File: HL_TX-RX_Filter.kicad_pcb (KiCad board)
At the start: 2 copper layers, 100 x 100 mm, 200 parts, among them J1 CNR1, J10 To Rx in, J11 CONN_01X03, J2 CNR3, J3 Antenna, J4 CNR2, J5 CNR4, J6 From Tx, J7 ICSP, J8 CONN_01X05, J9 SCL SDA, Q1 2N7002, Q2 2N7002, Q3 2N7002, Q4 2N7002, Q5 2N7002, Q6 2N7002, Q7 2N7002, Q8 2N7002, U1 ATMEGA328-AU, U10 PE4259, U11 PE4259, U12 PE4259, U2 PE4259, U3 PE4259, U4 PE4259, U5 PE4259, U6 PE4259, U7 PE4259, U8 PE4259, U9 PE4259

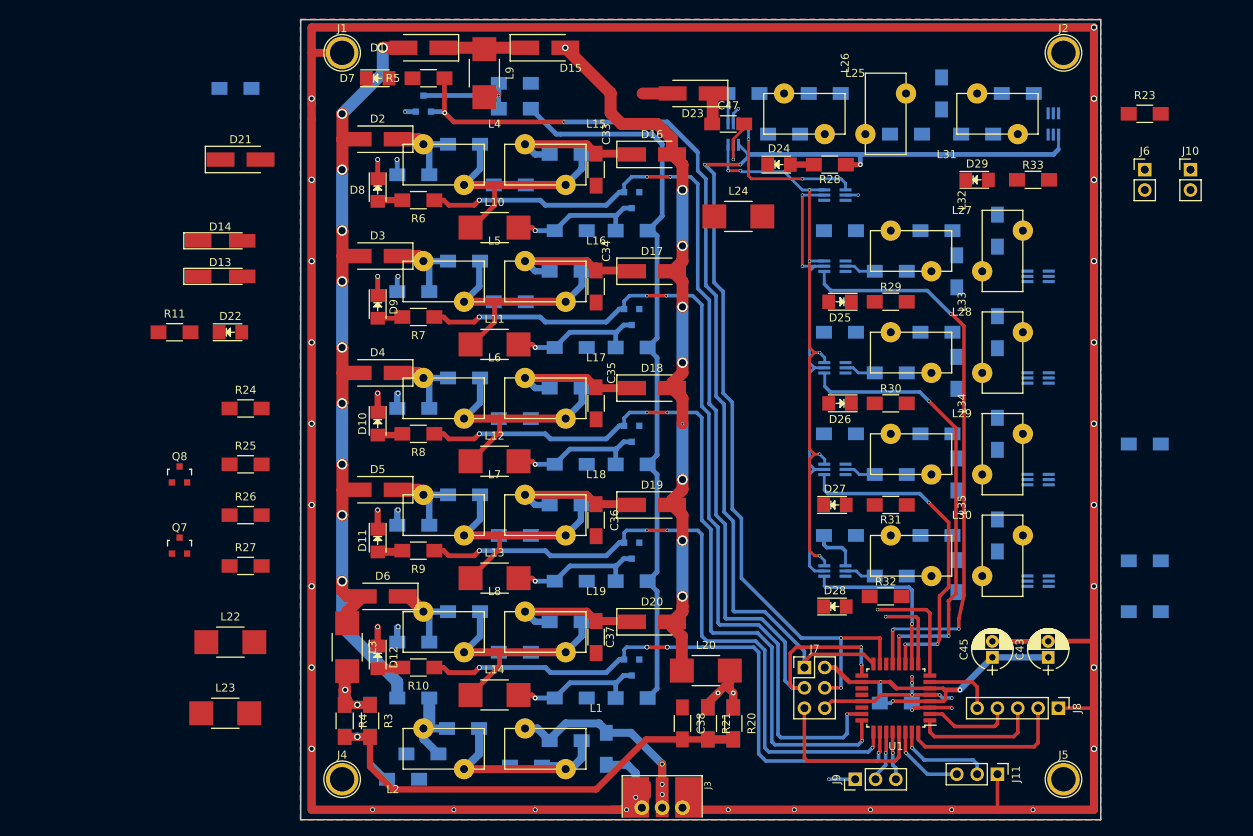
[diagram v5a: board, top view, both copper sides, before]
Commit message: Add Tx/Rx changeover components
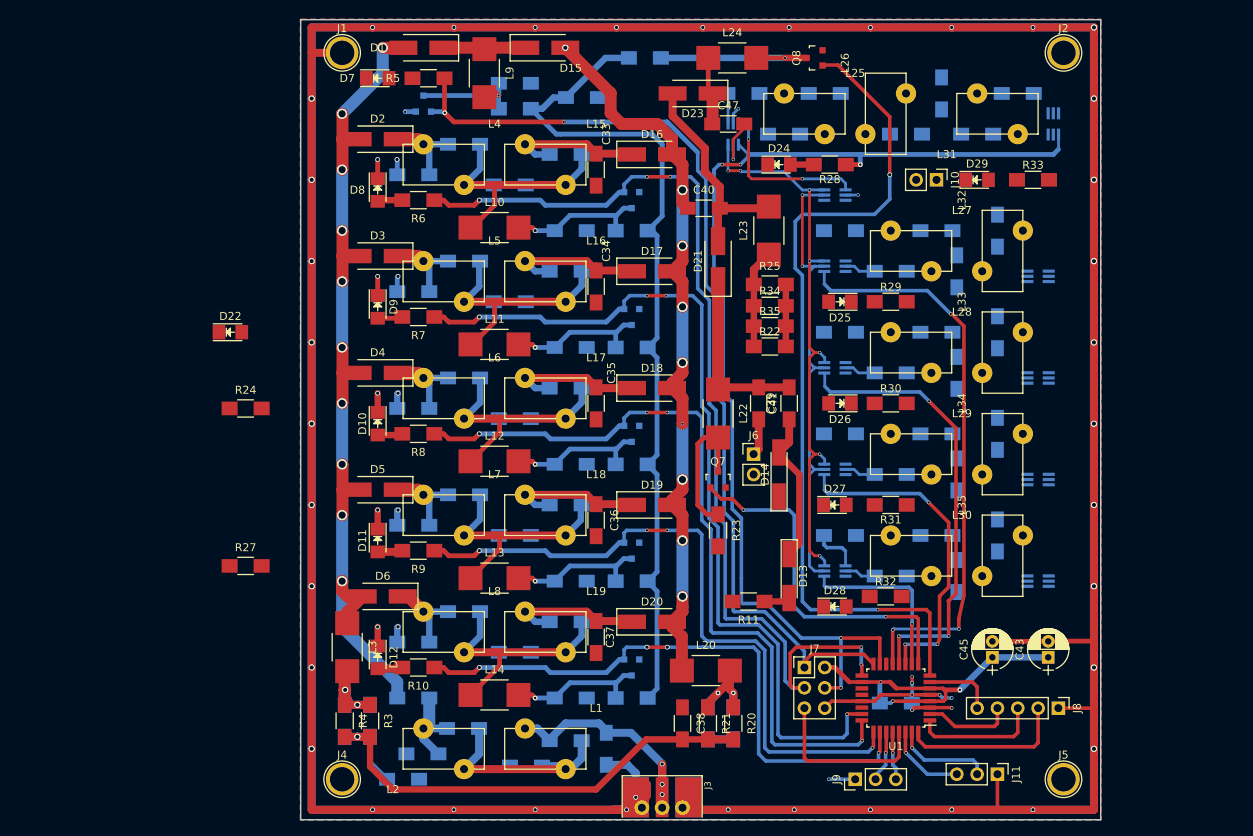
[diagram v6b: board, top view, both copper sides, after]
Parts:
- added R22: 680, Resistors_SMD:R_1206_HandSoldering, F.Cu at (183.6, 100.8)
- added R34: 680, Resistors_SMD:R_1206_HandSoldering, F.Cu at (183.6, 95.8)
- added R35: 680, Resistors_SMD:R_1206_HandSoldering, F.Cu at (183.6, 98.3)
- C39, C40, C41: moved to F.Cu
- R1, R18, R19, R2, R20, R21, R25, R3, R4: value R -> 680
- R26: moved to B.Cu
- moved Q8 94.9 mm to (189.2, 64.8), turned to 90 degrees
- moved C46 91.1 mm to (160.1, 69.7)
- moved L23 90.9 mm to (183.5, 86.4), turned to 90 degrees
- moved D13 80.4 mm to (186.1, 129.5), turned to 270 degrees
- moved C39 79.6 mm to (186.1, 108.0), turned to 90 degrees
- moved R11 79.3 mm to (181.0, 132.7), turned to 180 degrees
- moved R26 75.9 mm to (168.0, 64.8), turned to 180 degrees
- moved D14 75.7 mm to (184.8, 116.8), turned to 90 degrees
- moved R23 74.5 mm to (177.2, 123.8), turned to 270 degrees
- moved R25 69.3 mm to (183.6, 93.1)
- moved Q7 67.8 mm to (177.2, 117.5)
- moved L22 67.3 mm to (177.2, 109.2), turned to 270 degrees
- moved C40 62.5 mm to (175.4, 83.6)
- moved D21 61.0 mm to (177.2, 90.2), turned to 90 degrees
- moved J6 60.5 mm to (181.6, 114.3)
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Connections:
- C38 pad 2: Net-(C38-Pad2) -> BiasV
- C6 pad 2: Net-(C38-Pad2) -> BiasV
- L23 pad 1: 3V3 -> Net-(L23-Pad1)
- L23 pad 2: Net-(L23-Pad2) -> Net-(C40-Pad2)
- R1 pad 2: Net-(C38-Pad2) -> BiasV
- R18 pad 2: Net-(C38-Pad2) -> BiasV
- R19 pad 2: Net-(C38-Pad2) -> BiasV
- R2 pad 2: Net-(C38-Pad2) -> BiasV
- R20 pad 2: Net-(C38-Pad2) -> BiasV
- R21 pad 2: Net-(C38-Pad2) -> BiasV
- R25 pad 1: Net-(L23-Pad2) -> Net-(L23-Pad1)
- R25 pad 2: Net-(C40-Pad2) -> BiasV
- R3 pad 2: Net-(C38-Pad2) -> BiasV
- R4 pad 2: Net-(C38-Pad2) -> BiasV
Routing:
- net /Rptt: track 14.5 -> 106.6 mm, vias 1 -> 2
- net BiasV: track 0.00 -> 76.4 mm, vias 0 -> 1
- net Net-(C38-Pad2): track 68.7 -> 0.00 mm, vias 1 -> 0
- net /Tptt: track 9.83 -> 45.2 mm, vias 1 -> 2
- net Net-(C40-Pad2): track 3.75 -> 27.2 mm
- net Net-(C39-Pad2): track 0.00 -> 22.9 mm
- net Net-(L24-Pad2): track 0.00 -> 21.8 mm, vias 0 -> 1
- net Net-(C39-Pad1): track 0.00 -> 18.9 mm
- net Net-(L22-Pad2): track 0.00 -> 17.8 mm
- net Net-(C46-Pad1): track 92.4 -> 107.3 mm
- net Net-(L23-Pad1): track 0.00 -> 12.3 mm
- net Net-(C47-Pad1): track 3.83 -> 8.50 mm
- net Net-(C41-Pad2): track 0.00 -> 4.61 mm
- net Net-(D13-Pad2): track 0.00 -> 3.26 mm
- net Net-(C40-Pad1): track 91.1 -> 93.6 mm
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
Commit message: More layout around bias voltage area
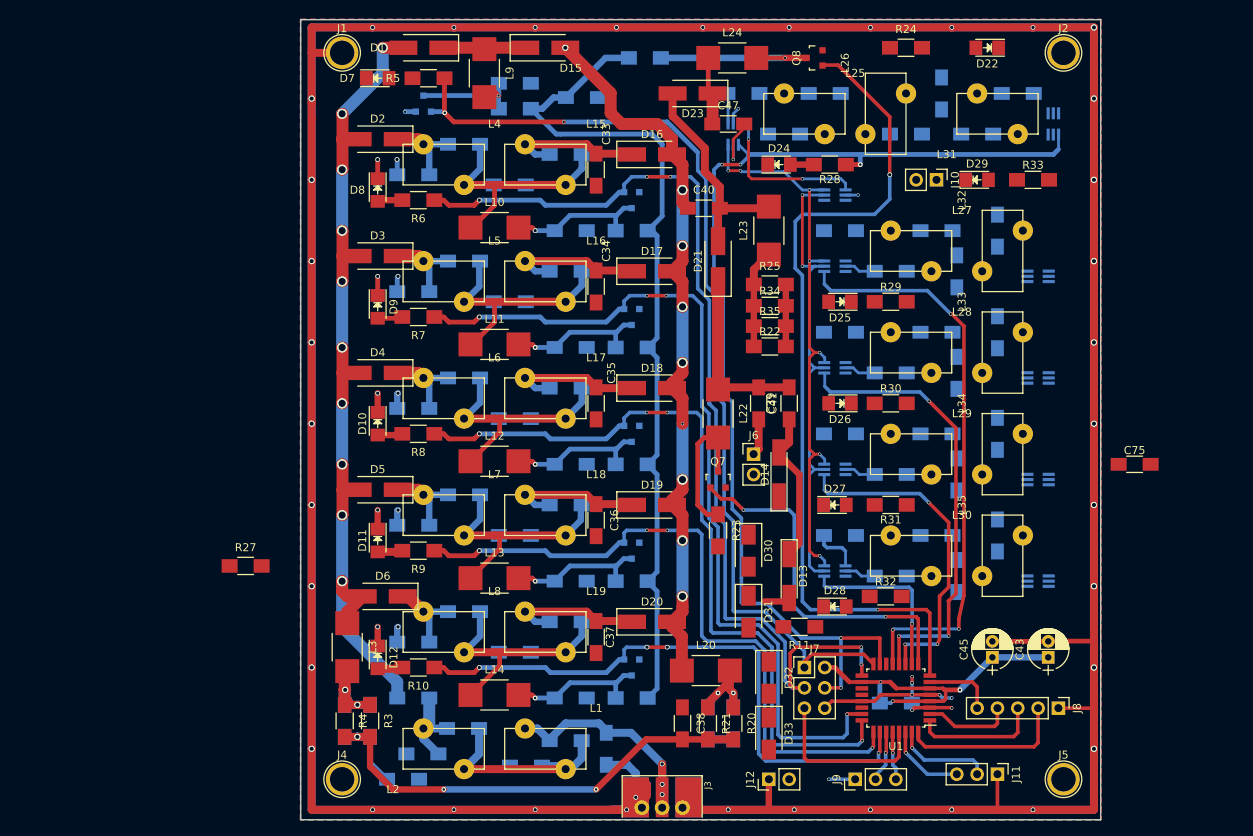
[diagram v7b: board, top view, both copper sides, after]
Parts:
- added C75: .1u, Capacitors_SMD:C_1206_HandSoldering, F.Cu at (229.2, 115.6)
- added D30: M7, Diodes_SMD:D_SMA, F.Cu at (181.0, 126.4)
- added D31: M7, Diodes_SMD:D_SMA, F.Cu at (181.0, 134.0)
- added D32: M7, Diodes_SMD:D_SMA, F.Cu at (183.5, 142.2)
- added D33: M7, Diodes_SMD:D_SMA, F.Cu at (183.5, 149.2)
- added J12: + - 12v, Pin_Headers:Pin_Header_Straight_1x02_Pitch2.54mm, F.Cu at (183.5, 154.9)
- moved D22 101.1 mm to (210.8, 63.5), turned to 180 degrees
- moved R24 94.1 mm to (200.7, 63.5)
- moved R11 7.10 mm to (187.3, 135.9)
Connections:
- R11 pad 2: +12V -> +12v
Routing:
- net GND: track 883.1 -> 886.9 mm
- net BiasV: vias 1 -> 3

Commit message: Got last of components placed on board
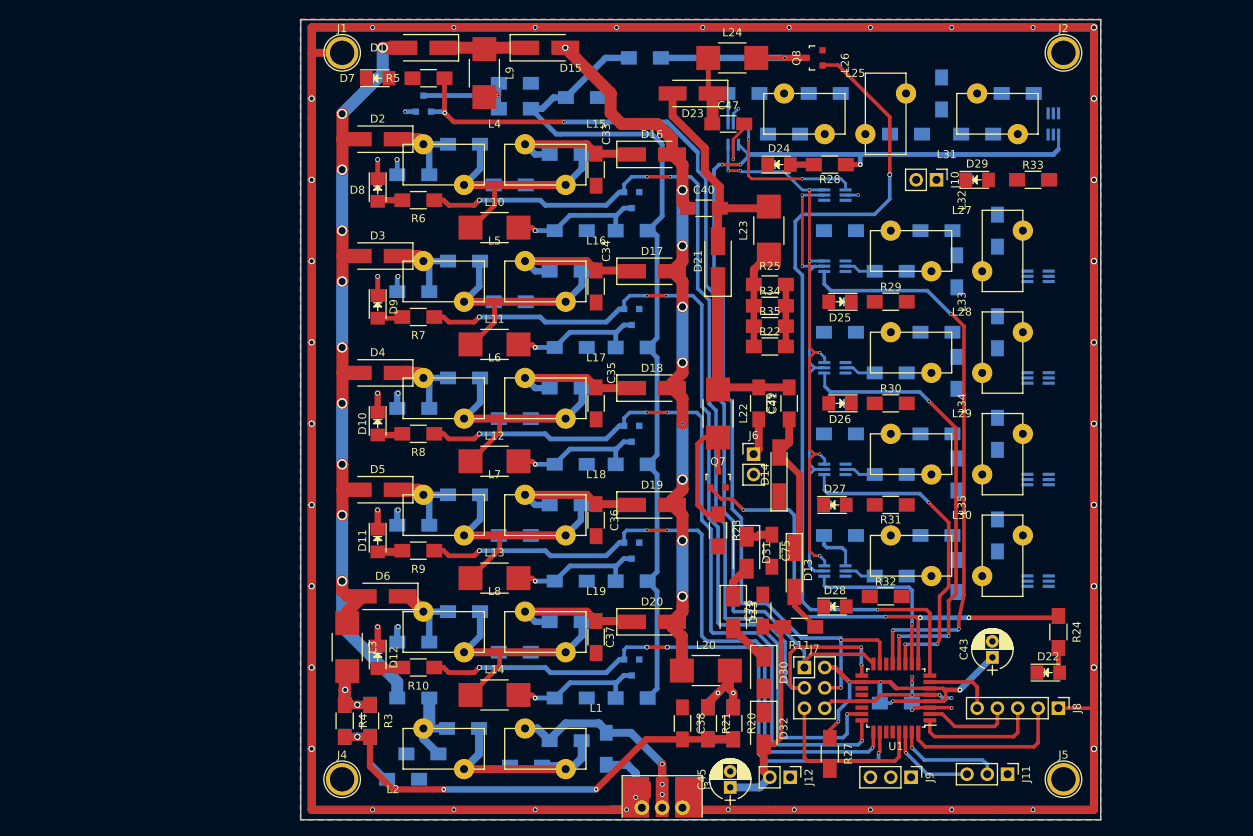
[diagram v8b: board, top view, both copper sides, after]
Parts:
- added C76: .1u, Capacitors_SMD:C_1206_HandSoldering, F.Cu at (182.8, 133.9)
- moved D22 78.5 mm to (218.4, 141.6), turned to 0 degrees
- moved R27 76.7 mm to (191.1, 151.8), turned to 270 degrees
- moved R24 75.5 mm to (219.7, 136.5), turned to 270 degrees
- moved C75 46.6 mm to (183.9, 126.4), turned to 270 degrees
- moved C45 36.6 mm to (178.7, 156.0)
- moved D33 15.8 mm to (179.1, 134.1)
- moved D30 15.4 mm to (182.9, 141.6)
- moved D31 7.37 mm to (180.7, 126.6)
- moved J9 6.99 mm to (201.3, 154.7), turned to 270 degrees
- moved C43 6.98 mm to (211.5, 139.7)
- moved D32 6.38 mm to (182.9, 148.6)
- moved J12 2.68 mm to (186.2, 154.7), turned to 270 degrees
- moved J11 1.27 mm to (213.4, 154.3)
- moved D13 0.99 mm to (186.7, 128.8)
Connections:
- C45 pad 1: 3V3 -> +12v
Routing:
- net +12v: track 0.00 -> 29.0 mm
- net GND: track 886.9 -> 862.3 mm, vias 59 -> 58
- net /Tptt: track 45.2 -> 63.0 mm, vias 2 -> 4
- net /SDA: track 6.47 -> 0.00 mm, vias 1 -> 0
- net /SCL: track 6.08 -> 0.00 mm, vias 1 -> 0
- net Net-(D30-Pad1): track 0.00 -> 5.26 mm
- net Net-(D31-Pad2): track 0.00 -> 4.18 mm
- net BiasV: track 76.4 -> 79.7 mm
- net Net-(D22-Pad2): track 0.00 -> 3.14 mm
- net Net-(D13-Pad2): track 3.26 -> 5.80 mm
- net Net-(C39-Pad1): track 18.9 -> 17.1 mm
- net /S1: track 10.1 -> 11.4 mm
- net /RESET: track 21.5 -> 22.8 mm
- net /S2: track 12.2 -> 13.5 mm
- net 3V3: track 115.0 -> 116.1 mm, vias 10 -> 12
